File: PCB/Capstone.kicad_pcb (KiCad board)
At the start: 4 copper layers, 86.4 x 68.6 mm, 238 parts, among them J1 S2B-PH-SM4-TB, J10 DNP, J11 DNP, J12 DNP, J2 TRANSDUCER, J3 DNP, J4 PH1-08-UA, J5 DNP, J6 DNP, J7 DNP, J8 PH1-08-UA, J9 DNP, Q1 SSM6K361NU, SW1 SW_Push, SW2 SW_Push, SW3 SW_Push, U1 TPS63031, U10 AP2204K-ADJ, U11 LM3478, U12 10CL010, U13 ECS-5032MV, U14 TSX9291, U15 LTC6090-5, U16 AD5450, U17 ADA4522-1, U18 MAX5394L, U19 MAX5394L, U2 TCR2EF25, U20 MAX11116, U21 TLV3544, U22 MCP6L1, U3 TPS62262, U4 BMD-360, U5 MIC841N, U6 ENS210, U7 W25Q80DV, U8 LIS2DE12, U9 LMR62421

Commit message: Tiny fixes to the schematic
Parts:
- J8: value PH1-08-UA -> DNP
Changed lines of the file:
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@@
       (effects (font (size 0.8 0.8) (thickness 0.05)))
     )
-    (fp_text value PH1-08-UA (at 0 20.11) (layer F.Fab)
+    (fp_text value DNP (at 0 20.11) (layer F.Fab)
       (effects (font (size 0.8 0.8) (thickness 0.05)))
     )

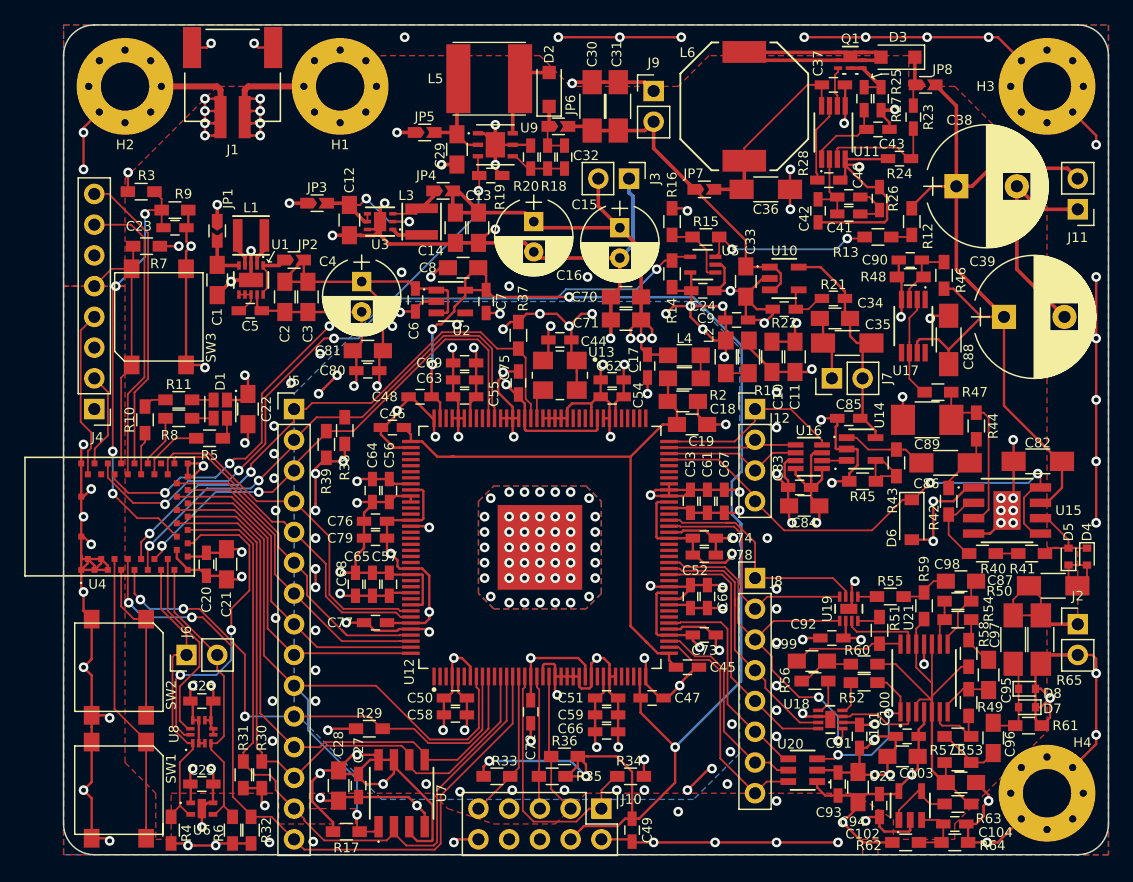
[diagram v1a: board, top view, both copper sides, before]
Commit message: Adjust design rules slightly, reroute affected traces
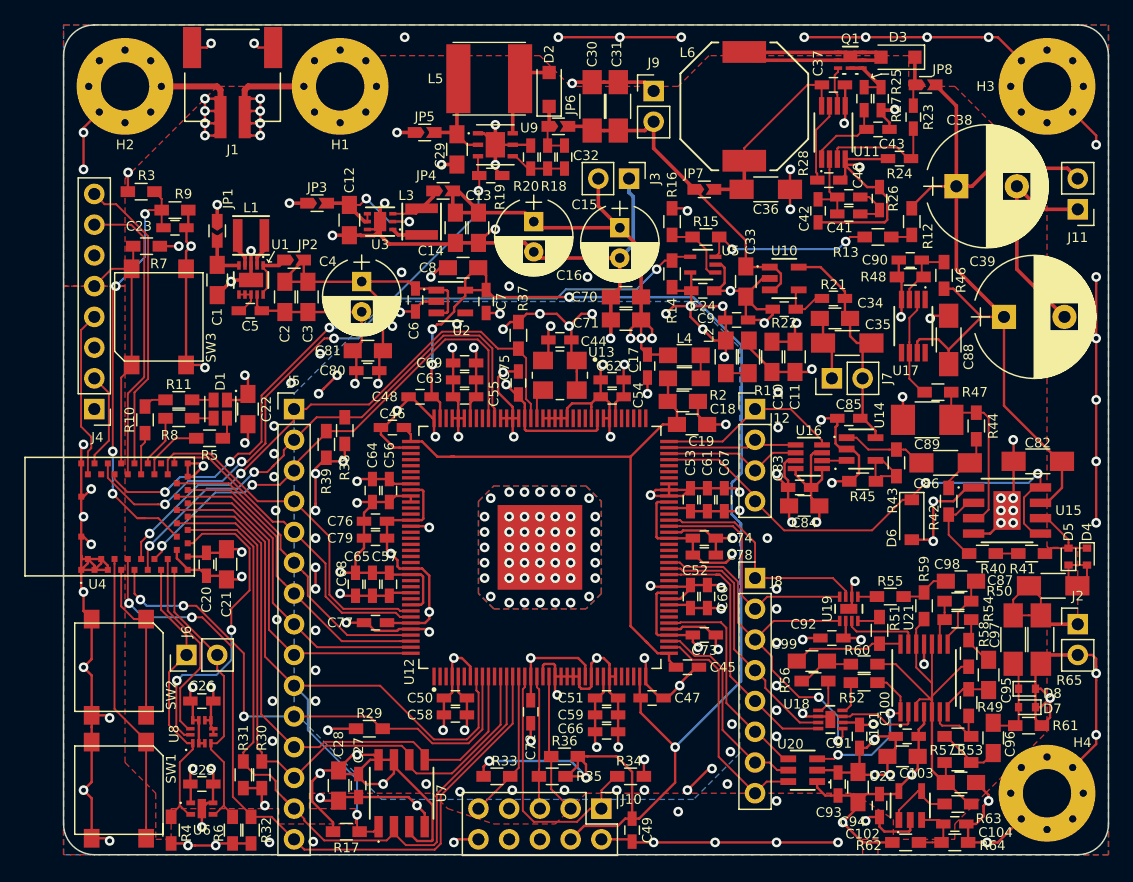
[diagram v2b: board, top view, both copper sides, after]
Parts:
- moved C53 0.13 mm to (138.2, 134.5)
- moved C61 0.13 mm to (139.6, 134.5)
- moved C67 0.13 mm to (141.0, 134.5)
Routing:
- net VGA-SCK: track 34.9 -> 32.7 mm
- net +2V5: track 123.4 -> 124.3 mm
- net VGA-~CS0: track 20.2 -> 19.2 mm
- net Net-(C23-Pad1): track 35.8 -> 36.4 mm
- net VGA-~CS1: track 21.8 -> 21.2 mm
- net FPGA-LINK2: track 26.7 -> 26.1 mm
- net DAC-~CS: track 15.8 -> 15.2 mm
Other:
- net class Default: clearance 0.15 -> 0.16; trace_width 0.15 -> 0.16
- net class Power: clearance 0.15 -> 0.16
- net class Signal50: trace_width 0.15 -> 0.16
- rule trace_clearance: 0.15 -> 0.16
- rule trace_min: 0.15 -> 0.16

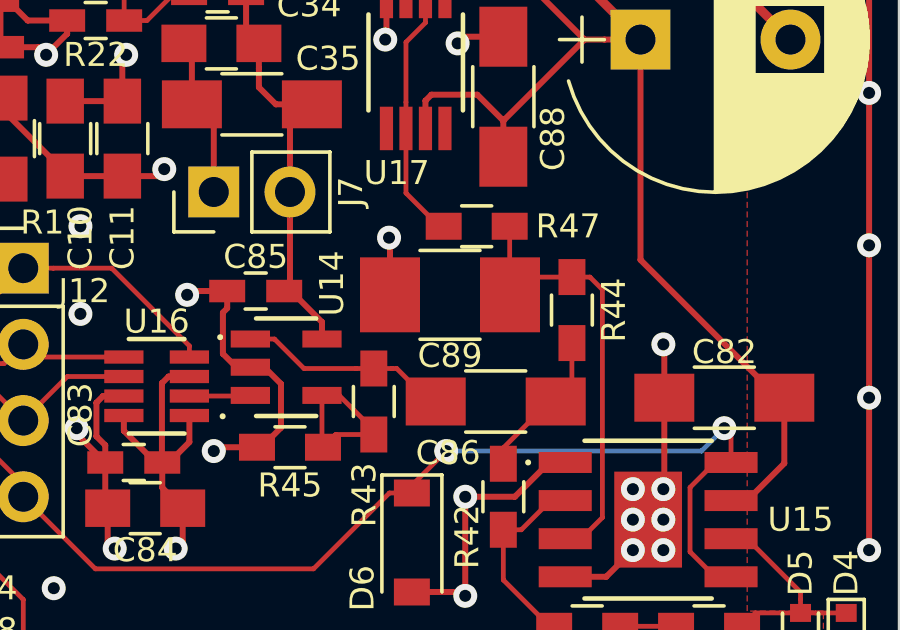
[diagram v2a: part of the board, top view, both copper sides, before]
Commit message: Fix incorrect footprint, begin organizing fabrication layer
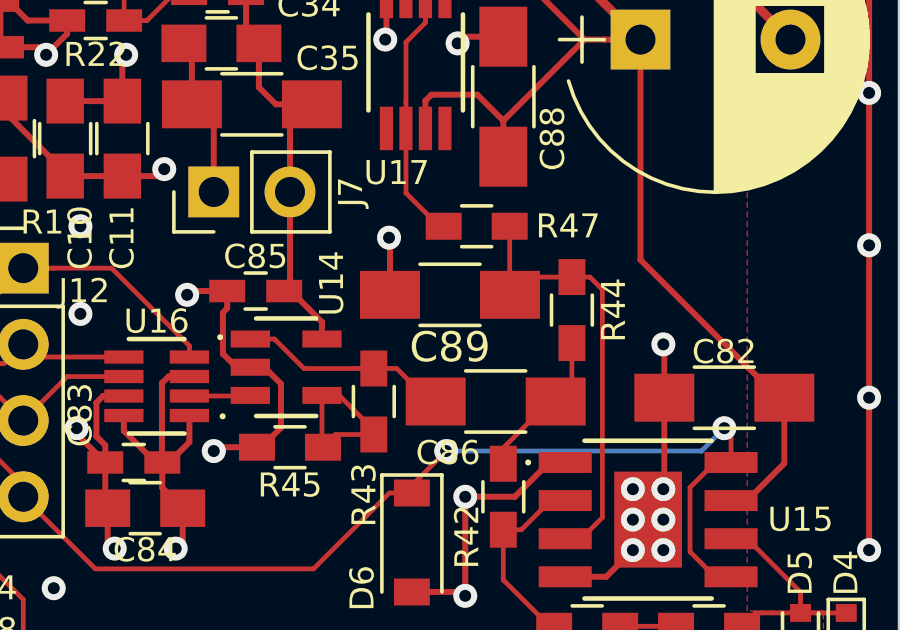
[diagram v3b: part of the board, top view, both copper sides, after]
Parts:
- C89: footprint Capacitors_SMD:C_1210_HandSoldering -> Capacitors_SMD:C_1206_HandSoldering

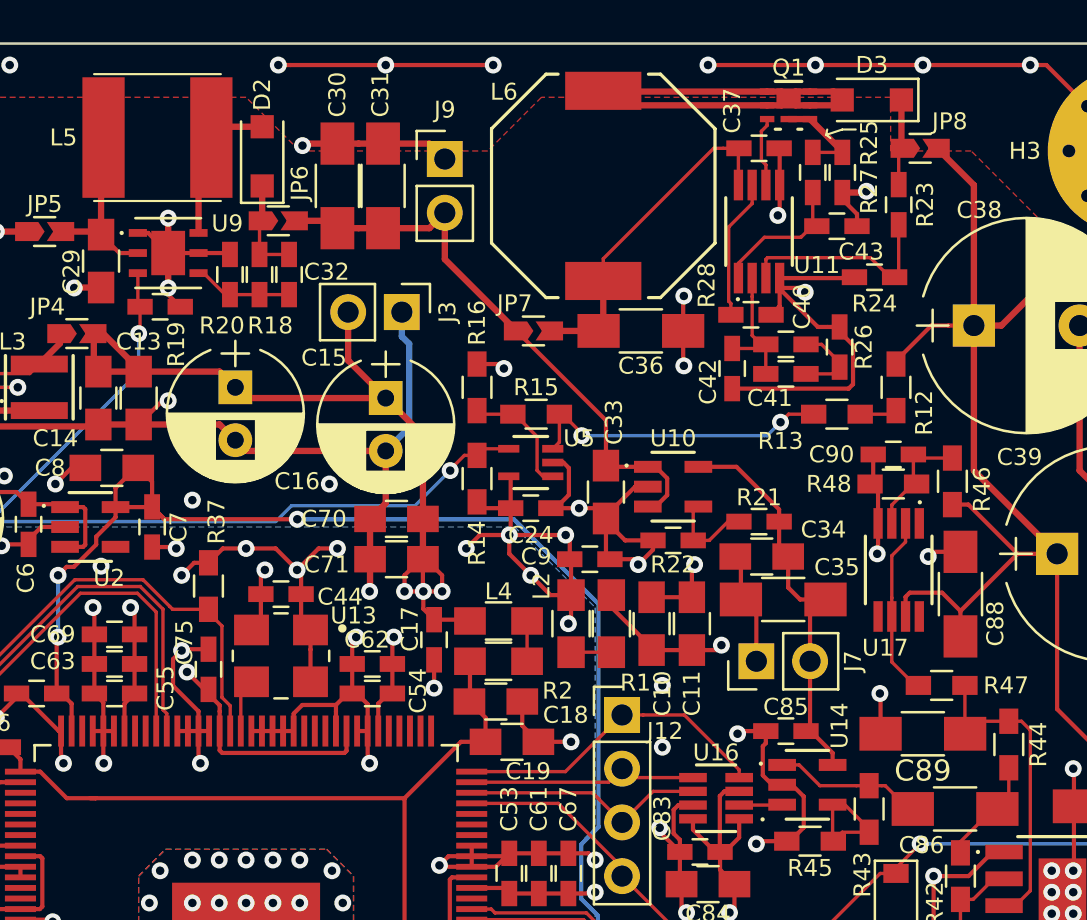
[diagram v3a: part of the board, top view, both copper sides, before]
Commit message: Fix resistors to use resistor footprints
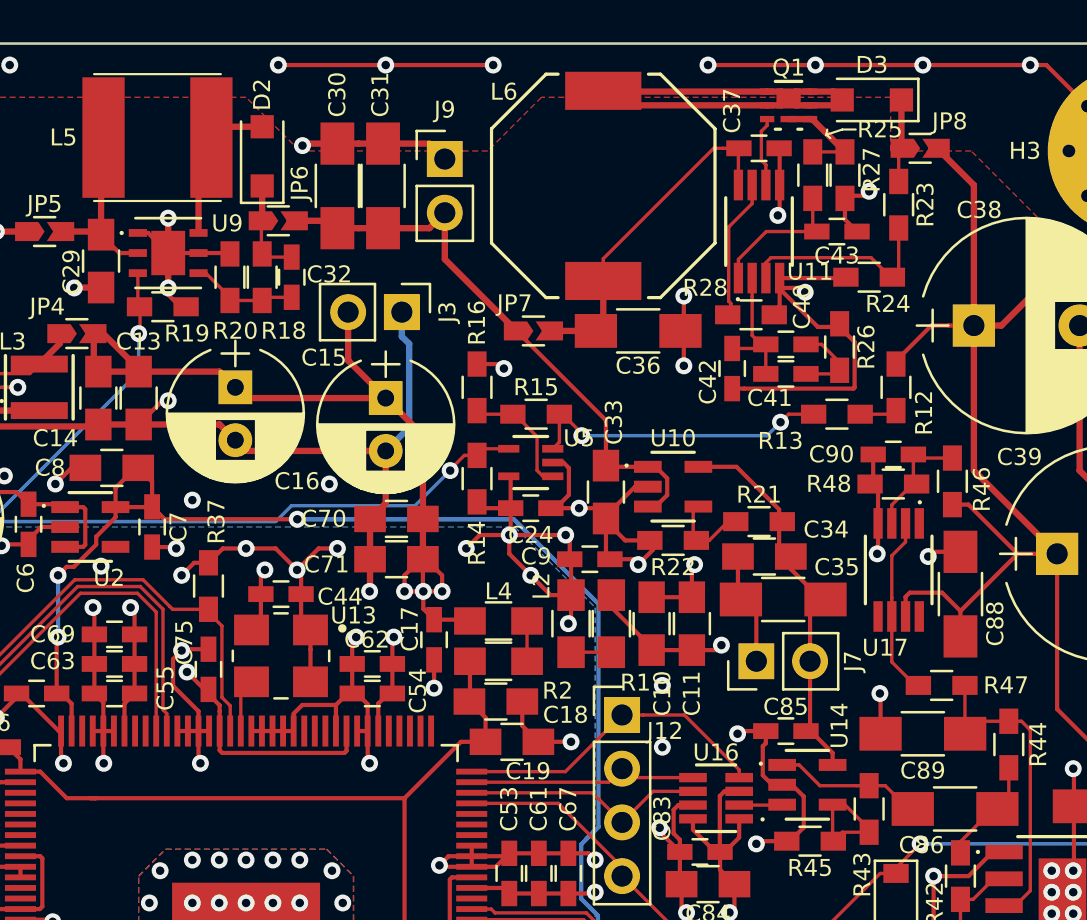
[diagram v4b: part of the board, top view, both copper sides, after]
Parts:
- R18, R19, R20, R21, R22, R23, R24, R25, R26, R27, R28: footprint Capacitors_SMD:C_0603_HandSoldering -> Resistors_SMD:R_0603_HandSoldering
- moved R24 0.25 mm to (155.2, 106.3)
- moved C43 0.25 mm to (153.7, 104.1)
- moved R18 0.18 mm to (126.5, 106.3)
- moved C32 0.18 mm to (127.9, 106.3)
- moved R27 0.18 mm to (154.1, 101.5)
- moved C34 0.13 mm to (150.2, 119.5)
- moved C36 0.13 mm to (144.3, 108.8)
- moved R19 0.13 mm to (121.8, 107.7)
- moved R20 0.13 mm to (125.0, 106.3)
- moved R25 0.13 mm to (152.5, 101.5)
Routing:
- net +10V: track 19.4 -> 18.7 mm

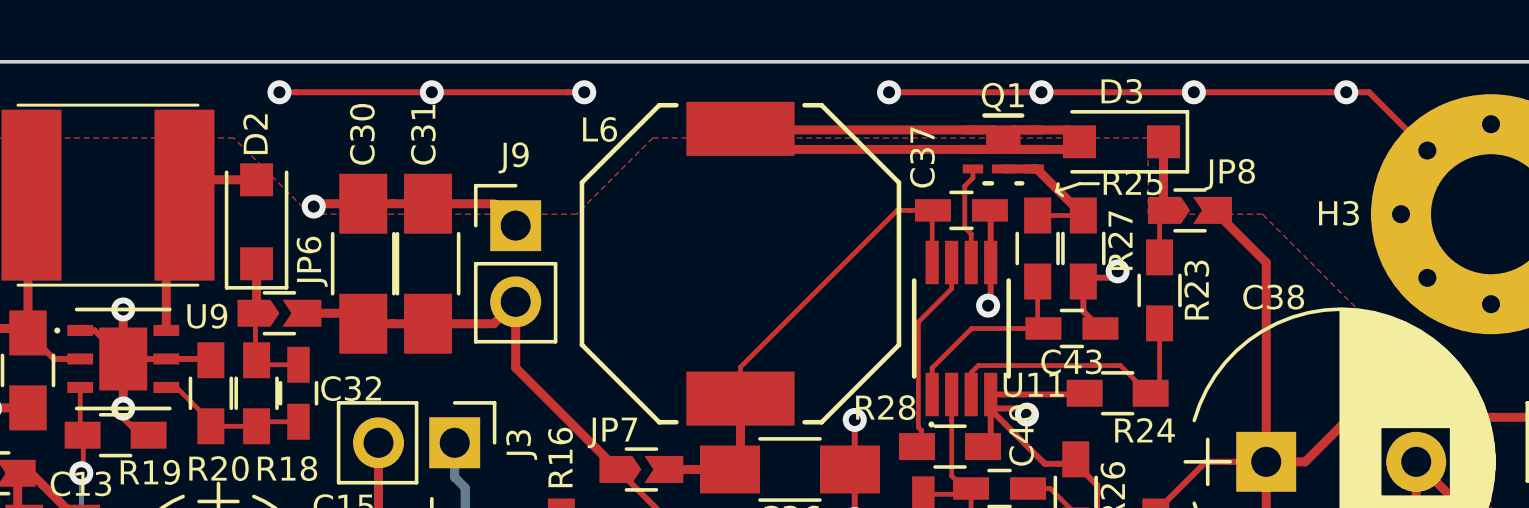
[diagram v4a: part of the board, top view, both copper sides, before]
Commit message: Fix incorrect footprint on power supply diodes
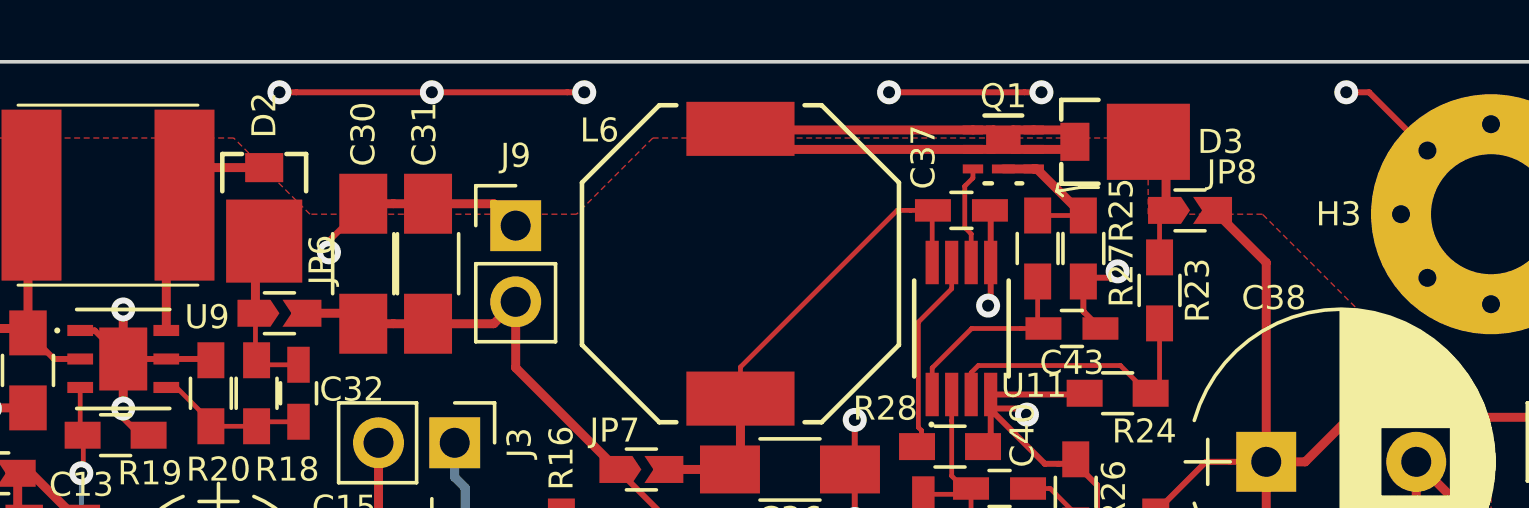
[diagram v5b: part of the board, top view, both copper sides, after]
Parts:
- D2, D3: footprint Diodes_SMD:D_SOD-123F -> Parts:DO-220AA
- moved D2 0.28 mm to (126.7, 100.5)
- moved D3 0.13 mm to (155.4, 97.9)
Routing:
- net GND: track 607.2 -> 597.5 mm, vias 204 -> 203
- net Net-(C32-Pad1): track 4.71 -> 5.57 mm
